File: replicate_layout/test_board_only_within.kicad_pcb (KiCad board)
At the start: 2 copper layers, 30 parts, among them J1001 Pusa_4mm, J1002 Pusa_4mm, Q1001 CSD19531KCS, Q1002 CSD19531KCS, Q1003 CSD19531KCS, Q2001 CSD19531KCS, Q2002 CSD19531KCS, Q3001 CSD19531KCS, Q3002 CSD19531KCS, Q4001 CSD19531KCS, Q4002 CSD19531KCS, U1001 LAUNCHXL-F28377S, U2001 IR2181, U3001 IR2181, U4001 IR2181

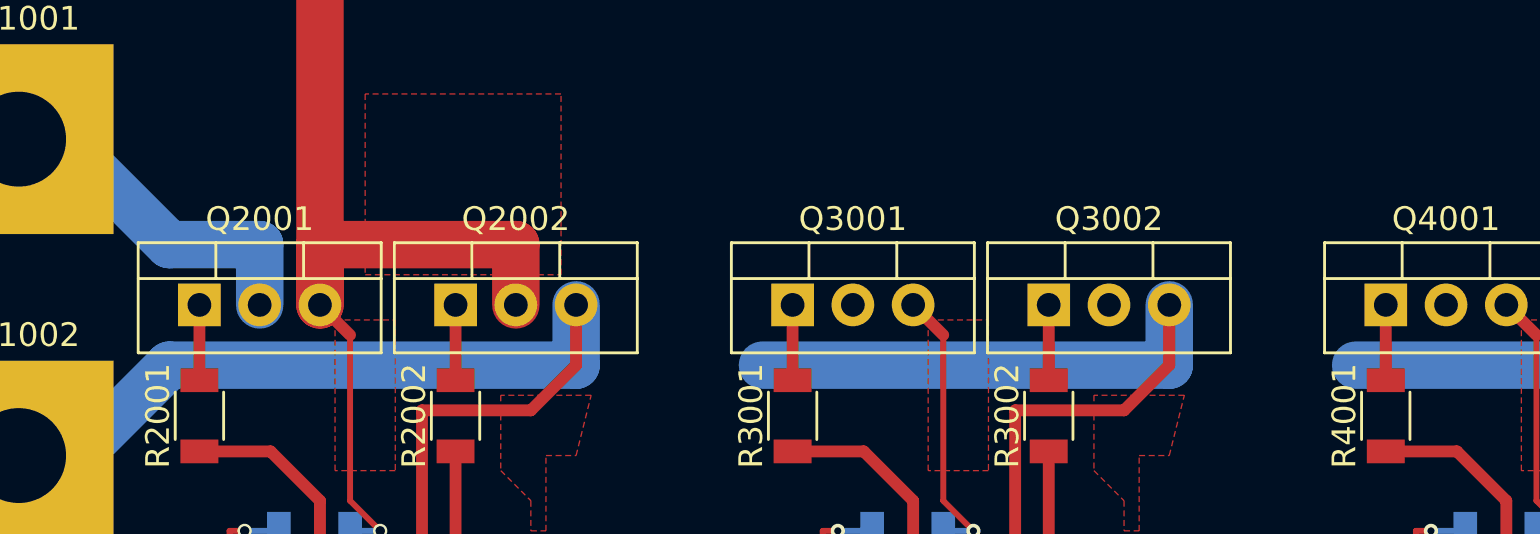
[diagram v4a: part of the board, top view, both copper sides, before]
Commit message: Added replication of tracks which are outside of bounding box but are on nets which are contained only within the sheet to be replicated.
updated test layouts.
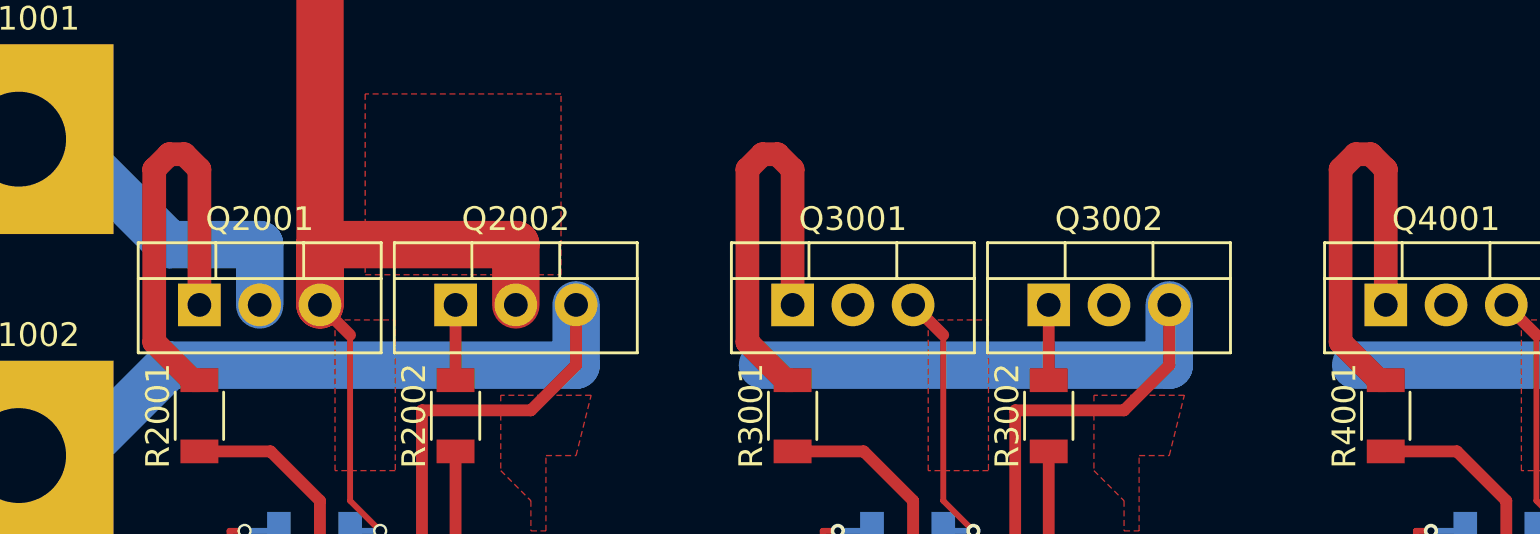
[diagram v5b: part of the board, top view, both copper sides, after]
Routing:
- net /Veja_3/QH_G: track 3.17 -> 18.0 mm
- net /Veja_2/QH_G: track 3.17 -> 18.0 mm
- net /Veja_1/QH_G: track 3.17 -> 18.0 mm
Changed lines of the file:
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@@
     (thickness 1.6)
     (drawings 0)
-    (tracks 133)
+    (tracks 151)
     (zones 0)
     (modules 30)
@@
   (segment (start 236.69 92.535) (end 236.69 101.29) (width 0.5) (layer F.Cu) (net 27))
   (segment (start 236.69 86.36) (end 236.69 89.535) (width 0.5) (layer F.Cu) (net 24))
-  (segment (start 225.895 86.36) (end 225.895 89.535) (width 0.5) (layer F.Cu) (net 23))
+  (segment (start 225.595 89.535) (end 223.99 87.93) (width 1) (layer F.Cu) (net 23))
+  (segment (start 225.895 89.535) (end 225.595 89.535) (width 1) (layer F.Cu) (net 23))
+  (segment (start 223.99 87.93) (end 223.99 80.645) (width 1) (layer F.Cu) (net 23))
+  (segment (start 223.99 80.645) (end 224.625 80.01) (width 1) (layer F.Cu) (net 23))
+  (segment (start 224.625 80.01) (end 225.26 80.01) (width 1) (layer F.Cu) (net 23))
+  (segment (start 225.895 80.645) (end 225.895 86.36) (width 1) (layer F.Cu) (net 23))
+  (segment (start 225.26 80.01) (end 225.895 80.645) (width 1) (layer F.Cu) (net 23))
   (segment (start 230.975 98.265) (end 230.975 94.615) (width 0.5) (layer F.Cu) (net 16))
   (segment (start 228.895 92.535) (end 225.895 92.535) (width 0.5) (layer F.Cu) (net 16))
@@
   (segment (start 211.69 92.535) (end 211.69 101.29) (width 0.5) (layer F.Cu) (net 26))
   (segment (start 211.69 86.36) (end 211.69 89.535) (width 0.5) (layer F.Cu) (net 22))
-  (segment (start 200.895 86.36) (end 200.895 89.535) (width 0.5) (layer F.Cu) (net 21))
+  (segment (start 200.595 89.535) (end 198.99 87.93) (width 1) (layer F.Cu) (net 21))
+  (segment (start 200.895 89.535) (end 200.595 89.535) (width 1) (layer F.Cu) (net 21))
+  (segment (start 198.99 87.93) (end 198.99 80.645) (width 1) (layer F.Cu) (net 21))
+  (segment (start 198.99 80.645) (end 199.625 80.01) (width 1) (layer F.Cu) (net 21))
+  (segment (start 199.625 80.01) (end 200.26 80.01) (width 1) (layer F.Cu) (net 21))
+  (segment (start 200.895 80.645) (end 200.895 86.36) (width 1) (layer F.Cu) (net 21))
+  (segment (start 200.26 80.01) (end 200.895 80.645) (width 1) (layer F.Cu) (net 21))
   (segment (start 205.975 98.265) (end 205.975 94.615) (width 0.5) (layer F.Cu) (net 15))
   (segment (start 203.895 92.535) (end 200.895 92.535) (width 0.5) (layer F.Cu) (net 15))
@@
   (segment (start 178.895 92.535) (end 175.895 92.535) (width 0.5) (layer F.Cu) (net 14))
   (segment (start 180.975 98.265) (end 180.975 94.615) (width 0.5) (layer F.Cu) (net 14))
-  (segment (start 175.895 86.36) (end 175.895 89.535) (width 0.5) (layer F.Cu) (net 19))
+  (segment (start 175.26 80.01) (end 175.895 80.645) (width 1) (layer F.Cu) (net 19))
+  (segment (start 175.895 80.645) (end 175.895 86.36) (width 1) (layer F.Cu) (net 19))
+  (segment (start 174.625 80.01) (end 175.26 80.01) (width 1) (layer F.Cu) (net 19))
+  (segment (start 173.99 80.645) (end 174.625 80.01) (width 1) (layer F.Cu) (net 19))
+  (segment (start 173.99 87.93) (end 173.99 80.645) (width 1) (layer F.Cu) (net 19))
+  (segment (start 175.895 89.535) (end 175.595 89.535) (width 1) (layer F.Cu) (net 19))
+  (segment (start 175.595 89.535) (end 173.99 87.93) (width 1) (layer F.Cu) (net 19))
   (segment (start 186.69 86.36) (end 186.69 89.535) (width 0.5) (layer F.Cu) (net 20))
   (segment (start 186.69 92.535) (end 186.69 101.29) (width 0.5) (layer F.Cu) (net 25))
